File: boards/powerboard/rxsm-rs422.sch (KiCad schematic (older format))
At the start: 8 parts, among them U701 MAX13432EESD

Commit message: [powerboard] BLDC motor controller
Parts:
- C701, C702: footprint (none) -> Capacitors_SMD:C_0603
- R701: footprint (none) -> Resistors_SMD:R_0603
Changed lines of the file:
@@
 LIBS:ds26lv32at
 LIBS:drv8312
+LIBS:drv8332
 LIBS:powerboard-cache
 EELAYER 25 0
@@
 F 0 "C702" H 6025 2250 50  0000 L CNN
 F 1 "100n" H 6025 2050 50  0000 L CNN
-F 2 "" H 6038 2000 50  0000 C CNN
+F 2 "Capacitors_SMD:C_0603" H 6038 2000 50  0001 C CNN
 F 3 "" H 6000 2150 50  0000 C CNN
 	1    6000 2150
@@
 F 0 "C701" H 4875 2250 50  0000 L CNN
 F 1 "100n" H 4650 2050 50  0000 L CNN
-F 2 "" H 4888 2000 50  0000 C CNN
+F 2 "Capacitors_SMD:C_0603" H 4888 2000 50  0001 C CNN
 F 3 "" H 4850 2150 50  0000 C CNN
 	1    4850 2150
@@
 F 0 "R701" V 4680 2400 50  0000 C CNN
 F 1 "10k" V 4600 2400 50  0000 C CNN
-F 2 "" V 4530 2400 50  0001 C CNN
+F 2 "Resistors_SMD:R_0603" V 4530 2400 50  0001 C CNN
 F 3 "" H 4600 2400 50  0001 C CNN
 	1    4600 2400

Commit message: [powerboard] selected all components and assigned all footprints
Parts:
- D701, D702: footprint (none) -> TO_SOT_Packages_SMD:SOT-23
- FL701, FL702: footprint (none) -> WE-SLx:WE-SL2
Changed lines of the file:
@@
 $EndComp
 $Comp
-L GND #PWR603
+L GND #PWR053
 U 1 1 58FF7E8F
 P 5550 3700
-F 0 "#PWR603" H 5550 3450 50  0001 C CNN
+F 0 "#PWR053" H 5550 3450 50  0001 C CNN
 F 1 "GND" H 5550 3550 50  0000 C CNN
 F 2 "" H 5550 3700 50  0000 C CNN
@@
 $EndComp
 $Comp
-L +3V3 #PWR601
+L +3V3 #PWR054
 U 1 1 58FF7E95
 P 4600 2100
-F 0 "#PWR601" H 4600 1950 50  0001 C CNN
+F 0 "#PWR054" H 4600 1950 50  0001 C CNN
 F 1 "+3V3" H 4600 2240 50  0000 C CNN
 F 2 "" H 4600 2100 50  0000 C CNN
@@
 $EndComp
 $Comp
-L +5V #PWR604
+L +5V #PWR055
 U 1 1 58FF7E9B
 P 6150 2300
-F 0 "#PWR604" H 6150 2150 50  0001 C CNN
+F 0 "#PWR055" H 6150 2150 50  0001 C CNN
 F 1 "+5V" H 6150 2440 50  0000 C CNN
 F 2 "" H 6150 2300 50  0000 C CNN
@@
 F 0 "FL701" H 6100 2755 60  0000 C CNB
 F 1 "CMC" H 6100 2440 45  0000 C CNN
-F 2 "" H 6100 2375 40  0001 C CNN
+F 2 "WE-SLx:WE-SL2" H 6100 2375 40  0001 C CNN
 F 3 "" H 6100 2750 60  0000 C CNN
 F 4 "-" H 6100 2835 45  0001 C CNN "PART"
@@
 F 0 "FL702" H 6100 3255 60  0000 C CNB
 F 1 "CMC" H 6100 2940 45  0000 C CNN
-F 2 "" H 6100 2875 40  0001 C CNN
+F 2 "WE-SLx:WE-SL2" H 6100 2875 40  0001 C CNN
 F 3 "" H 6100 3250 60  0000 C CNN
 F 4 "-" H 6100 3335 45  0001 C CNN "PART"
@@
 2x Farnell #1735590
 $Comp
-L GND #PWR605
+L GND #PWR056
 U 1 1 58FF7EC2
 P 6550 1900
-F 0 "#PWR605" H 6550 1650 50  0001 C CNN
+F 0 "#PWR056" H 6550 1650 50  0001 C CNN
 F 1 "GND" H 6550 1750 50  0000 C CNN
 F 2 "" H 6550 1900 50  0000 C CNN
@@
 F 0 "D701" H 6380 2270 39  0000 C CNN
 F 1 "ESD" H 6400 2050 39  0000 C CNN
-F 2 "" H 6400 2150 39  0001 C CNN
+F 2 "TO_SOT_Packages_SMD:SOT-23" H 6400 2150 39  0001 C CNN
 F 3 "" H 6400 2150 39  0001 C CNN
 	1    6400 2150
@@
 F 0 "D702" H 6650 2250 39  0000 C CNN
 F 1 "ESD" H 6700 2050 39  0000 C CNN
-F 2 "" H 6700 2150 39  0001 C CNN
+F 2 "TO_SOT_Packages_SMD:SOT-23" H 6700 2150 39  0001 C CNN
 F 3 "" H 6700 2150 39  0001 C CNN
 	1    6700 2150
@@
 $EndComp
 $Comp
-L GND #PWR602
+L GND #PWR057
 U 1 1 58FF7EDD
 P 5400 2000
-F 0 "#PWR602" H 5400 1750 50  0001 C CNN
+F 0 "#PWR057" H 5400 1750 50  0001 C CNN
 F 1 "GND" H 5400 1850 50  0000 C CNN
 F 2 "" H 5400 2000 50  0000 C CNN

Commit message: [powerboard] select inductors, assign footprints; import netlist in PCB
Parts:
- U701: footprint SOIC_Packages:SOIC-14_3.9x8.7mm_Pitch1.27mm -> Housings_SOIC:SOIC-14_3.9x8.7mm_Pitch1.27mm
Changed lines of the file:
@@
 F 0 "U701" H 5050 3550 50  0000 L CNN
 F 1 "MAX13432EESD" H 5750 3550 50  0000 R CNN
-F 2 "SOIC_Packages:SOIC-14_3.9x8.7mm_Pitch1.27mm" H 5400 1900 50  0001 C CIN
+F 2 "Housings_SOIC:SOIC-14_3.9x8.7mm_Pitch1.27mm" H 5400 1900 50  0001 C CIN
 F 3 "" H 5400 3700 50  0001 C CNN
 	1    5400 2900

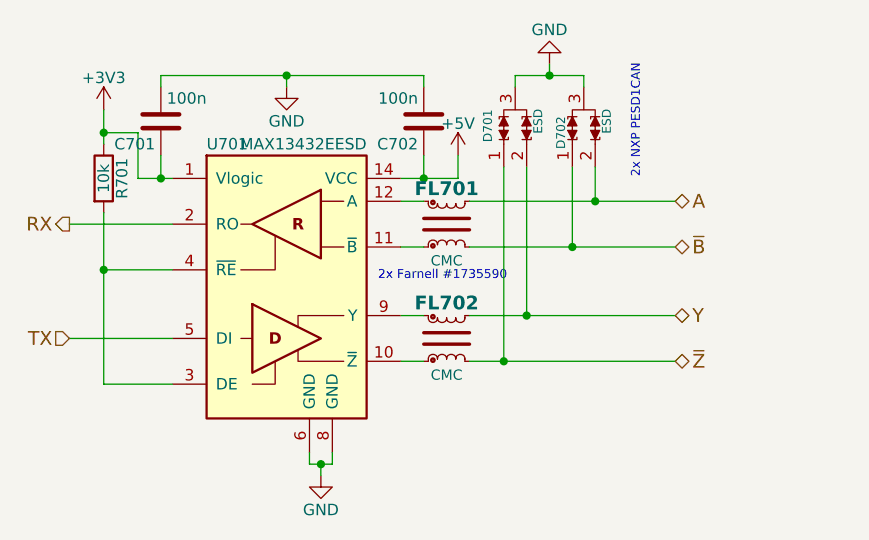
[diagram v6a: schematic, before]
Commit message: [powerboard] layout: parts placed; RS-422 termination added; various minor improvements
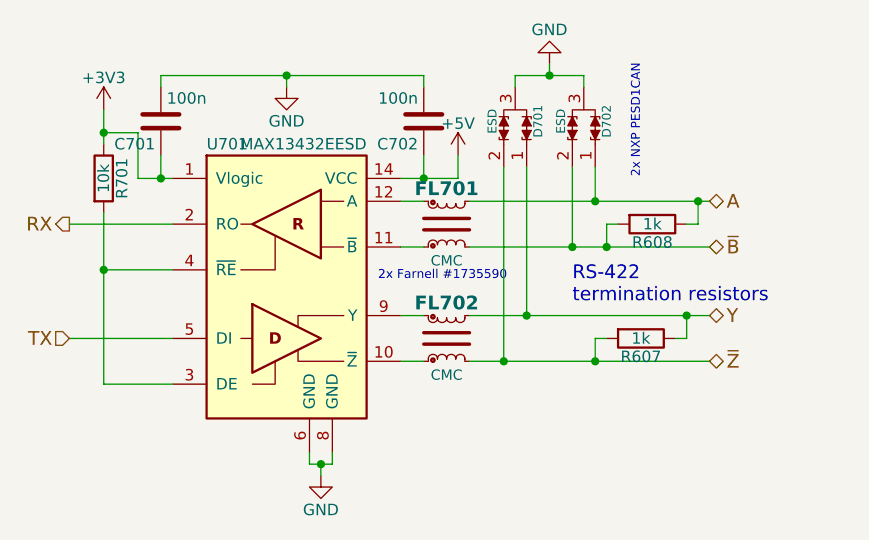
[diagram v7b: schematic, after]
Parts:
- added R607, R608: 1k, Resistors_SMD:R_0603, symbol R
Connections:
- net A: now also D702.1, R608.1; no longer D702.2
- net Y: now also D701.1, R607.1; no longer D701.2
- net ~B: now also D702.2, R608.2; no longer D702.1
- net ~Z: now also D701.2, R607.2; no longer D701.1
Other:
- note added: "RS-422\ntermination resistors"
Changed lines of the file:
@@
 $EndComp
 $Comp
-L GND #PWR053
+L GND #PWR055
 U 1 1 58FF7E8F
 P 5550 3700
-F 0 "#PWR053" H 5550 3450 50  0001 C CNN
+F 0 "#PWR055" H 5550 3450 50  0001 C CNN
 F 1 "GND" H 5550 3550 50  0000 C CNN
 F 2 "" H 5550 3700 50  0000 C CNN
@@
 $EndComp
 $Comp
-L +3V3 #PWR054
+L +3V3 #PWR056
 U 1 1 58FF7E95
 P 4600 2100
-F 0 "#PWR054" H 4600 1950 50  0001 C CNN
+F 0 "#PWR056" H 4600 1950 50  0001 C CNN
 F 1 "+3V3" H 4600 2240 50  0000 C CNN
 F 2 "" H 4600 2100 50  0000 C CNN
@@
 $EndComp
 $Comp
-L +5V #PWR055
+L +5V #PWR057
 U 1 1 58FF7E9B
 P 6150 2300
-F 0 "#PWR055" H 6150 2150 50  0001 C CNN
+F 0 "#PWR057" H 6150 2150 50  0001 C CNN
 F 1 "+5V" H 6150 2440 50  0000 C CNN
 F 2 "" H 6150 2300 50  0000 C CNN
@@
 2x Farnell #1735590
 $Comp
-L GND #PWR056
+L GND #PWR058
 U 1 1 58FF7EC2
 P 6550 1900
-F 0 "#PWR056" H 6550 1650 50  0001 C CNN
+F 0 "#PWR058" H 6550 1650 50  0001 C CNN
 F 1 "GND" H 6550 1750 50  0000 C CNN
 F 2 "" H 6550 1900 50  0000 C CNN
@@
 U 1 1 58FF7EC8
 P 6400 2150
-F 0 "D701" H 6380 2270 39  0000 C CNN
+F 0 "D701" H 6400 2250 39  0000 C CNN
 F 1 "ESD" H 6400 2050 39  0000 C CNN
 F 2 "TO_SOT_Packages_SMD:SOT-23" H 6400 2150 39  0001 C CNN
 F 3 "" H 6400 2150 39  0001 C CNN
 	1    6400 2150
-	0    -1   -1   0
+	0    1    -1   0
 $EndComp
 $Comp
@@
 U 1 1 58FF7ECF
 P 6700 2150
-F 0 "D702" H 6650 2250 39  0000 C CNN
+F 0 "D702" H 6700 2250 39  0000 C CNN
 F 1 "ESD" H 6700 2050 39  0000 C CNN
 F 2 "TO_SOT_Packages_SMD:SOT-23" H 6700 2150 39  0001 C CNN
 F 3 "" H 6700 2150 39  0001 C CNN
 	1    6700 2150
-	0    -1   -1   0
+	0    1    -1   0
 $EndComp
 $Comp
@@
 $EndComp
 $Comp
-L GND #PWR057
+L GND #PWR059
 U 1 1 58FF7EDD
 P 5400 2000
-F 0 "#PWR057" H 5400 1750 50  0001 C CNN
+F 0 "#PWR059" H 5400 1750 50  0001 C CNN
 F 1 "GND" H 5400 1850 50  0000 C CNN
 F 2 "" H 5400 2000 50  0000 C CNN
@@
 Connection ~ 6550 1950
 Wire Wire Line
-	6200 3200 7100 3200
-Wire Wire Line
-	6200 3000 7100 3000
-Wire Wire Line
-	6200 2700 7100 2700
-Wire Wire Line
-	6200 2500 7100 2500
+	6200 3200 7250 3200
+Wire Wire Line
+	6200 3000 7250 3000
+Wire Wire Line
+	6200 2700 7250 2700
+Wire Wire Line
+	6200 2500 7250 2500
 Wire Wire Line
 	6750 2350 6750 2500
@@
 	4600 3300 4900 3300
 Connection ~ 4600 2800
-Text HLabel 7100 2500 2    60   BiDi ~ 0
+Text HLabel 7250 2500 2    60   BiDi ~ 0
 A
-Text HLabel 7100 2700 2    60   BiDi ~ 0
+Text HLabel 7250 2700 2    60   BiDi ~ 0
 ~B
-Text HLabel 7100 3000 2    60   BiDi ~ 0
+Text HLabel 7250 3000 2    60   BiDi ~ 0
 Y
-Text HLabel 7100 3200 2    60   BiDi ~ 0
+Text HLabel 7250 3200 2    60   BiDi ~ 0
 ~Z
+$Comp
+L R R608
+U 1 1 5944BD36
+P 7000 2600
+F 0 "R608" V 7080 2600 50  0000 C CNN
+F 1 "1k" V 7000 2600 50  0000 C CNN
+F 2 "Resistors_SMD:R_0603" V 6930 2600 50  0001 C CNN
+F 3 "" H 7000 2600 50  0001 C CNN
+	1    7000 2600
+	0    1    1    0
+$EndComp
+$Comp
+L R R607
+U 1 1 5944BEA9
+P 6950 3100
+F 0 "R607" V 7030 3100 50  0000 C CNN
+F 1 "1k" V 6950 3100 50  0000 C CNN
+F 2 "Resistors_SMD:R_0603" V 6880 3100 50  0001 C CNN
+F 3 "" H 6950 3100 50  0001 C CNN
+	1    6950 3100
+	0    1    1    0
+$EndComp
+Wire Wire Line
+	7100 3100 7150 3100
+Wire Wire Line
+	7150 3100 7150 3000
+Connection ~ 7150 3000
+Wire Wire Line
+	6800 3100 6750 3100
+Wire Wire Line
+	6750 3100 6750 3200
+Connection ~ 6750 3200
+Wire Wire Line
+	6850 2600 6800 2600
+Wire Wire Line
+	6800 2600 6800 2700
+Connection ~ 6800 2700
+Wire Wire Line
+	7150 2600 7200 2600
+Wire Wire Line
+	7200 2600 7200 2500
+Connection ~ 7200 2500
+Text Notes 6650 2950 0    60   ~ 0
+RS-422\ntermination resistors
 $EndSCHEMATC
